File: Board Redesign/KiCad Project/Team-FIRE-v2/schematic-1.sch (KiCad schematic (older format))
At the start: 32 parts, among them J1 SIM_Card, J2 53885-0408, U2 NCN4555MN, U3 CSD18543Q3A

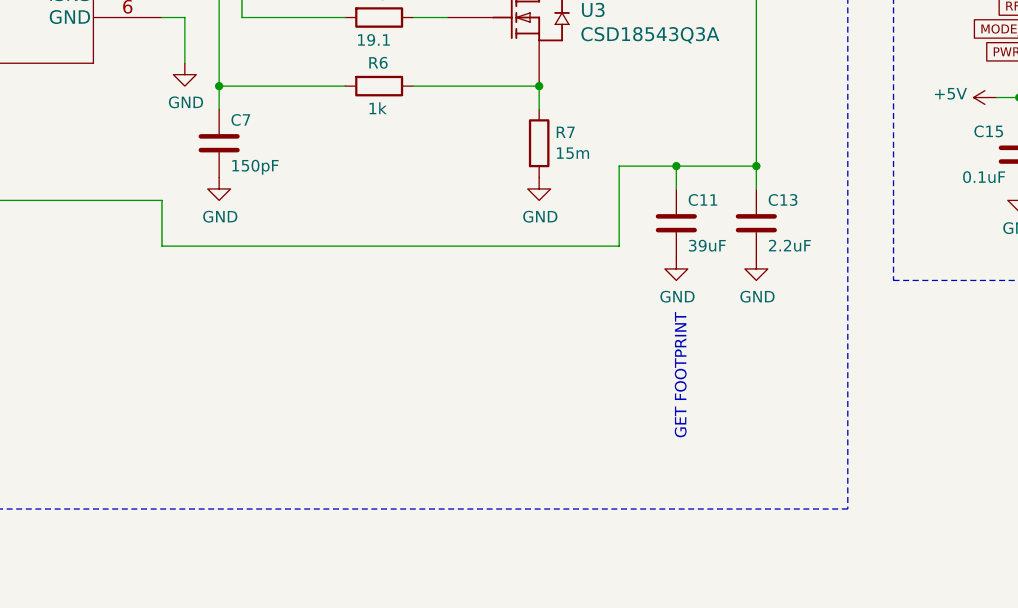
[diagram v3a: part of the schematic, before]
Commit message: Added EEE-FK1H390SV
- Created EEE-FK1H390SV symbol and footprint
- Added EEE-FK1H390SV to Team-FIRE libraries
- Added EEE-FK1H390SV to 8 to 30V boost circuit
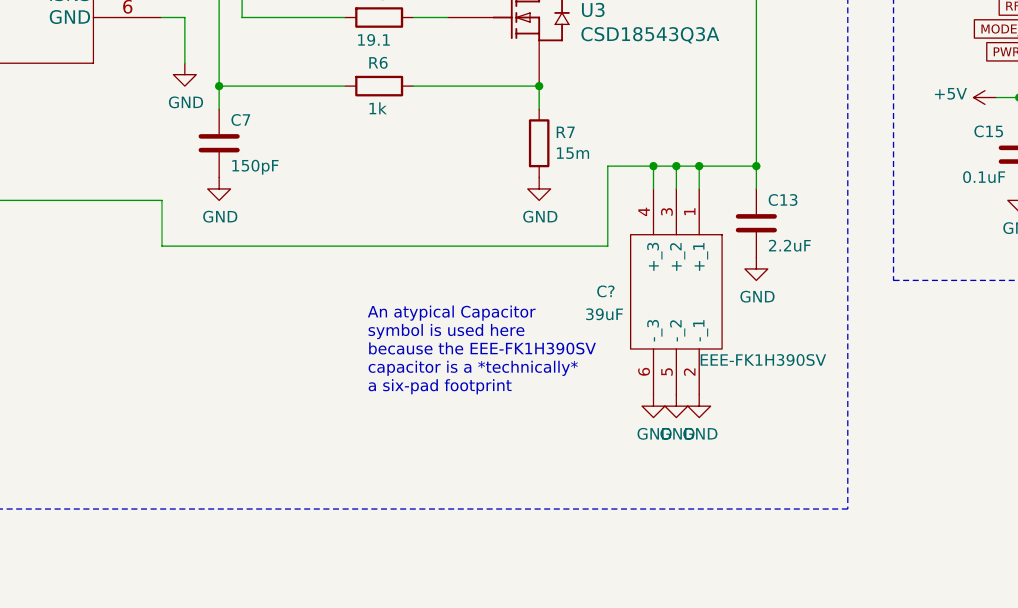
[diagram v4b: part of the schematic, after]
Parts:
- removed C11: 39uF, symbol Device:C
- added C?: 39uF, Team-FIRE:EEEFK1H390SV, symbol Team-FIRE:EEE-FK1H390SV
- C13: Link (none) -> https://www.mouser.com/ProductDetail/Murata-Electronics/GRM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; MPN (none) -> GRM188R61H225KE11D; Manufacturer (none) -> Murata; Supplier (none) -> Mouser; Supplier PN (none) -> 81-GRM188R61H225KE1D; Type (none) -> Ceramic X5R Capacitor; Voltage Rating (none) -> 50 VDC
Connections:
- net GND: now also C?.2 (-_1), C?.5 (-_2), C?.6 (-_3)
- net at C13.1, D1.1 (K), R4.2: now also C?.1 (+_1), C?.3 (+_2), C?.4 (+_3)
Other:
- note added: "An atypical Capacitor\nsymbol is used here\nbecause the EEE-FK1H390SV\ncapacitor is a *technically*\na six-pad footprint"
- note removed: "GET FOOTPRINT"
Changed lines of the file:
@@
-$EndComp
-$Comp
-L Device:C C11
-U 1 1 5ED7F879
-P 6100 3550
-F 0 "C11" H 6150 3650 50  0000 L CNN
-F 1 "39uF" H 6150 3450 50  0000 L CNN
-F 2 "" H 6138 3400 50  0001 C CNN
-F 3 "https://www.mouser.com/datasheet/2/315/ABA0000C1247-1144552.pdf" H 6100 3550 50  0001 C CNN
-F 4 "EEE-FK1H390SV" H 6100 3550 50  0001 C CNN "MPN"
-F 5 "Panasonic" H 6100 3550 50  0001 C CNN "Manufacturer"
-F 6 "Mouser" H 6100 3550 50  0001 C CNN "Supplier"
-F 7 "667-EEE-FK1H390SV" H 6100 3550 50  0001 C CNN "Supplier PN"
-F 8 "https://www.mouser.com/ProductDetail/Panasonic/EEE-FK1H390SV?qs=sGAEpiMZZMsh%252B1woXyUXj34sxNWs20QAUY71LHOgMEw%3D" H 6100 3550 50  0001 C CNN "Link"
-F 9 "Aluminum Electrolytic Capacitors" H 6100 3550 50  0001 C CNN "Type"
-F 10 "20%" H 6100 3550 50  0001 C CNN "Tolerance"
-F 11 "50 VDC" H 6100 3550 50  0001 C CNN "Voltage Rating"
-F 12 "AEC-Q200" H 6100 3550 50  0001 C CNN "Qualification"
-	1    6100 3550
-	1    0    0    -1
 $EndComp
 $Comp
@@
 F 1 "2.2uF" H 6500 3450 50  0000 L CNN
 F 2 "Capacitor_SMD:C_0603_1608Metric" H 6488 3400 50  0001 C CNN
-F 3 "~" H 6450 3550 50  0001 C CNN
+F 3 "https://www.mouser.com/datasheet/2/281/murata_03052018_GRM_Series_1-1310166.pdf" H 6450 3550 50  0001 C CNN
+F 4 "GRM188R61H225KE11D" H 6450 3550 50  0001 C CNN "MPN"
+F 5 "Murata" H 6450 3550 50  0001 C CNN "Manufacturer"
+F 6 "Mouser" H 6450 3550 50  0001 C CNN "Supplier"
+F 7 "81-GRM188R61H225KE1D" H 6450 3550 50  0001 C CNN "Supplier PN"
+F 8 "https://www.mouser.com/ProductDetail/Murata-Electronics/GRM188R61H225KE11D?qs=sGAEpiMZZMs0AnBnWHyRQKFZIQ7b73cd5p1cvIMBXrTOTAbV%2F8mfyA%3D%3D" H 6450 3550 50  0001 C CNN "Link"
+F 9 "Ceramic X5R Capacitor" H 6450 3550 50  0001 C CNN "Type"
+F 10 "50 VDC" H 6450 3550 50  0001 C CNN "Voltage Rating"
 	1    6450 3550
 	1    0    0    -1
@@
 L power:GND #PWR0123
 U 1 1 5ED80FA2
-P 6100 3700
-F 0 "#PWR0123" H 6100 3450 50  0001 C CNN
-F 1 "GND" H 6105 3527 50  0000 C CNN
-F 2 "" H 6100 3700 50  0001 C CNN
-F 3 "" H 6100 3700 50  0001 C CNN
-	1    6100 3700
+P 6100 4300
+F 0 "#PWR0123" H 6100 4050 50  0001 C CNN
+F 1 "GND" H 6105 4127 50  0000 C CNN
+F 2 "" H 6100 4300 50  0001 C CNN
+F 3 "" H 6100 4300 50  0001 C CNN
+	1    6100 4300
 	1    0    0    -1
 $EndComp
@@
 Connection ~ 6100 3300
 Wire Wire Line
-	6100 3300 6450 3300
+	6100 3300 6200 3300
 Wire Wire Line
 	6200 2200 6450 2200
@@
 Wire Wire Line
 	3950 2650 3850 2650
-Text Notes 6150 4500 1    50   ~ 0
-GET FOOTPRINT
 Connection ~ 4100 2950
 Wire Wire Line
@@
 	3850 3450 3850 3650
 Wire Wire Line
-	3850 3650 5850 3650
-Wire Wire Line
-	5850 3650 5850 3300
-Wire Wire Line
-	5850 3300 6100 3300
+	3850 3650 5800 3650
+Wire Wire Line
+	5800 3650 5800 3300
 Wire Wire Line
 	2650 3450 3850 3450
@@
 Text Notes 5450 6100 2    50   ~ 0
 FIND COMPONENT
+$Comp
+L Team-FIRE:EEE-FK1H390SV C?
+U 1 1 5EAA6D91
+P 6500 3400
+F 0 "C?" V 6950 2650 50  0000 L CNN
+F 1 "39uF" V 7050 2600 50  0000 L CNN
+F 2 "Team-FIRE:EEEFK1H390SV" H 7250 3500 50  0001 L CNN
+F 3 "https://b2b-api.panasonic.eu/file_stream/pids/fileversion/3102" H 7250 3400 50  0001 L CNN
+F 4 "667-EEE-FK1H390SV" H 7250 3100 50  0001 L CNN "Supplier PN"
+F 5 "Panasonic" H 7250 2900 50  0001 L CNN "Manufacturer"
+F 6 "EEE-FK1H390SV" V 7250 3100 50  0000 L CNN "MPN"
+F 7 "Digikey" H 6500 3400 50  0001 C CNN "Supplier"
+F 8 "https://www.digikey.com/product-detail/en/panasonic-electronic-components/EEE-FK1H390SV/P124697CT-ND/10290639" H 6500 3400 50  0001 C CNN "Link"
+F 9 "Aluminum Electrolytic Capacitor" H 6500 3400 50  0001 C CNN "Type"
+F 10 "20%" H 6500 3400 50  0001 C CNN "Tolerance"
+F 11 "50 VDC" H 6500 3400 50  0001 C CNN "Voltage Rating"
+	1    6500 3400
+	0    1    1    0
+$EndComp
+Wire Wire Line
+	6000 3400 6000 3300
+Connection ~ 6000 3300
+Wire Wire Line
+	6000 3300 6100 3300
+Wire Wire Line
+	6200 3400 6200 3300
+Connection ~ 6200 3300
+Wire Wire Line
+	6200 3300 6450 3300
+$Comp
+L power:GND #PWR?
+U 1 1 5EAC5511
+P 6000 4300
+F 0 "#PWR?" H 6000 4050 50  0001 C CNN
+F 1 "GND" H 6005 4127 50  0000 C CNN
+F 2 "" H 6000 4300 50  0001 C CNN
+F 3 "" H 6000 4300 50  0001 C CNN
+	1    6000 4300
+	1    0    0    -1
+$EndComp
+$Comp
+L power:GND #PWR?
+U 1 1 5EAC5A93
+P 6200 4300
+F 0 "#PWR?" H 6200 4050 50  0001 C CNN
+F 1 "GND" H 6205 4127 50  0000 C CNN
+F 2 "" H 6200 4300 50  0001 C CNN
+F 3 "" H 6200 4300 50  0001 C CNN
+	1    6200 4300
+	1    0    0    -1
+$EndComp
+Text Notes 4750 4300 0    50   ~ 0
+An atypical Capacitor\nsymbol is used here\nbecause the EEE-FK1H390SV\ncapacitor is a *technically*\na six-pad footprint
+Wire Wire Line
+	5800 3300 6000 3300
 $EndSCHEMATC

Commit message: Made a lot of changes...
- Added symbol, footprint for Micro USB B connector
- Fixed Flash Memory schematic
- Added details for many components
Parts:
- gave numbers to parts that had none: 4
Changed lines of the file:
@@
 	10550 1200 10650 1200
 $Comp
-L Team-FIRE:TPS40210DGQR U?
+L Team-FIRE:TPS40210DGQR U1
 U 1 1 5EAFAF05
 P 1850 2250
-F 0 "U?" H 2850 2637 60  0000 C CNN
+F 0 "U1" H 2850 2637 60  0000 C CNN
 F 1 "TPS40210DGQR" H 2850 2531 60  0000 C CNN
 F 2 "Team-FIRE:TPS40210DGQR" H 2950 2450 60  0001 C CNN
@@
 P 8900 5200
 AR Path="/5F173878" Ref="C?"  Part="1"
-AR Path="/5E4D0D8F/5F173878" Ref="C?"  Part="1"
+AR Path="/5E4D0D8F/5F173878" Ref="C12"  Part="1"
 AR Path="/5E759307/5F173878" Ref="C?"  Part="1"
-F 0 "C?" H 8750 5300 50  0000 L CNN
+F 0 "C12" H 8750 5300 50  0000 L CNN
 F 1 "1uF" H 8750 5100 50  0000 L CNN
 F 2 "Capacitor_SMD:C_0603_1608Metric" H 8938 5050 50  0001 C CNN
@@
 $EndComp
 $Comp
-L Device:C C?
+L Device:C C14
 U 1 1 5F174FB5
 P 9200 5200
-F 0 "C?" H 9250 5300 50  0000 L CNN
+F 0 "C14" H 9250 5300 50  0000 L CNN
 F 1 "10uF" H 9250 5100 50  0000 L CNN
 F 2 "Capacitor_SMD:C_0603_1608Metric" H 9238 5050 50  0001 C CNN
@@
 FIND COMPONENT
 $Comp
-L Team-FIRE:EEE-FK1H390SV C?
+L Team-FIRE:EEE-FK1H390SV C11
 U 1 1 5EAA6D91
 P 6500 3400
-F 0 "C?" V 6950 2650 50  0000 L CNN
+F 0 "C11" V 6950 2650 50  0000 L CNN
 F 1 "39uF" V 7050 2600 50  0000 L CNN
 F 2 "Team-FIRE:EEEFK1H390SV" H 7250 3500 50  0001 L CNN
@@
 	6200 3300 6450 3300
 $Comp
-L power:GND #PWR?
+L power:GND #PWR01
 U 1 1 5EAC5511
 P 6000 4300
-F 0 "#PWR?" H 6000 4050 50  0001 C CNN
+F 0 "#PWR01" H 6000 4050 50  0001 C CNN
 F 1 "GND" H 6005 4127 50  0000 C CNN
 F 2 "" H 6000 4300 50  0001 C CNN
@@
 $EndComp
 $Comp
-L power:GND #PWR?
+L power:GND #PWR02
 U 1 1 5EAC5A93
 P 6200 4300
-F 0 "#PWR?" H 6200 4050 50  0001 C CNN
+F 0 "#PWR02" H 6200 4050 50  0001 C CNN
 F 1 "GND" H 6205 4127 50  0000 C CNN
 F 2 "" H 6200 4300 50  0001 C CNN

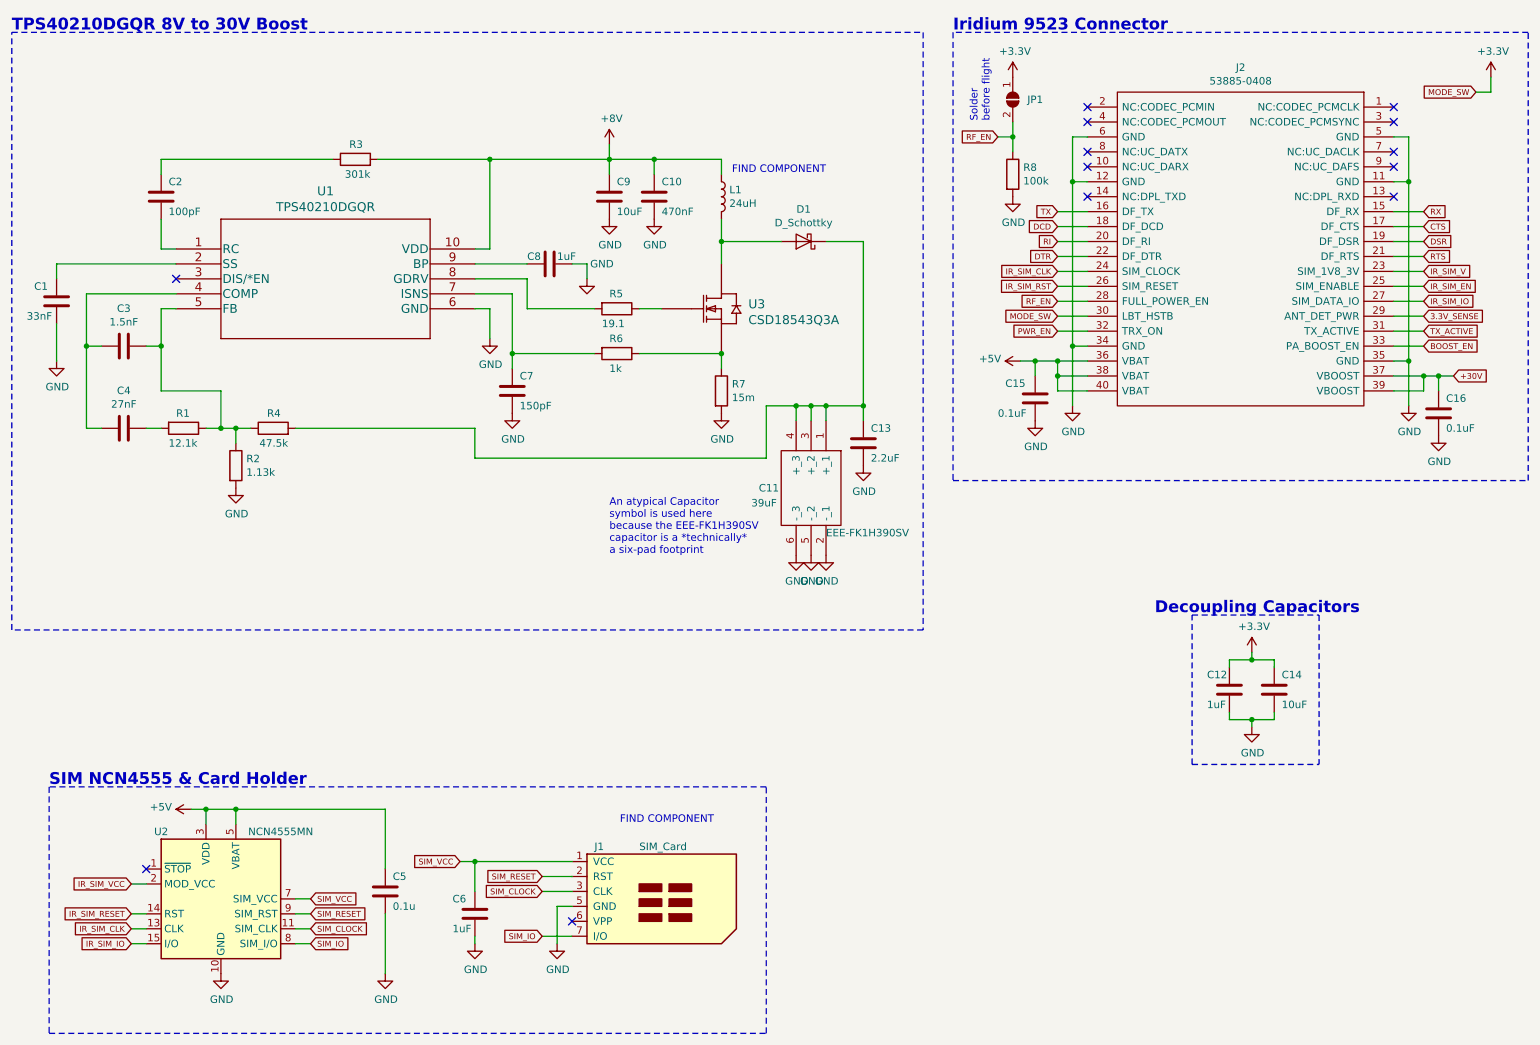
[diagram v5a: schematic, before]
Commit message: Labelled finished sections on schematic, picked LEDs
- Labelled all finished schematic sections if they've been part-selected / verified (and by whom)
- Selected the four debug LEDs and filled out BOM info
- Filled out info for Power/TES connectors
- Filled out info for RF connector
- Filled out info for 5 to 3.3V regulator
- Filled out info for 8 to 5V switching regulator
- Assigned footprints to test points
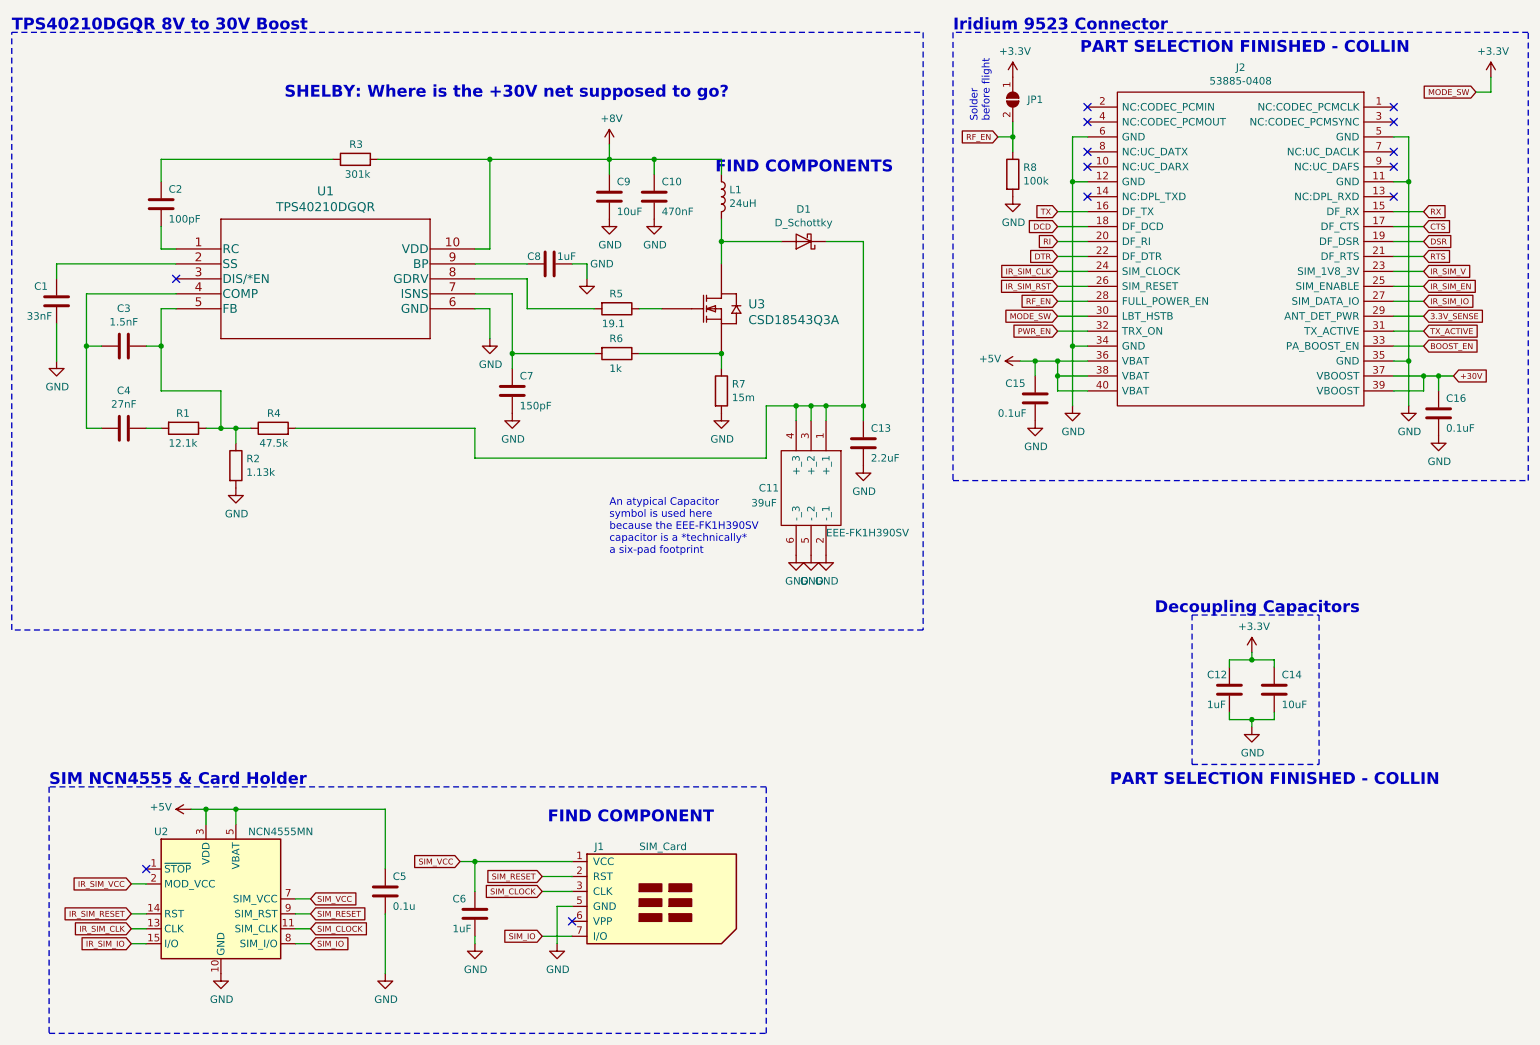
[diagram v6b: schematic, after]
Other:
- note added: "FIND COMPONENTS"
- note added: "PART SELECTION FINISHED - COLLIN"
- note added: "SHELBY: Where is the +30V net supposed to go?"
- moved on the sheet: C2
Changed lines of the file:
@@
 L Device:C C2
 U 1 1 5EA803DA
-P 1750 1900
-F 0 "C2" H 1800 2000 50  0000 L CNN
-F 1 "100pF" H 1800 1800 50  0000 L CNN
-F 2 "Capacitor_SMD:C_0603_1608Metric" H 1788 1750 50  0001 C CNN
-F 3 "~" H 1750 1900 50  0001 C CNN
-F 4 "CBR06C101F5GAC" H 1750 1900 50  0001 C CNN "MPN"
-F 5 "KEMET" H 1750 1900 50  0001 C CNN "Manufacturer"
-F 6 "https://www.mouser.com/ProductDetail/KEMET/CBR06C101F5GAC?qs=sGAEpiMZZMs0AnBnWHyRQN7%2FAA2D2lPPUdZo0nHgvrj7UthX3WhjQw%3D%3D" H 1750 1900 50  0001 C CNN "Link"
-F 7 "80-CBR06C101F5GAC" H 1750 1900 50  0001 C CNN "Supplier PN"
-F 8 "Ceramic C0G Capacitor" H 1750 1900 50  0001 C CNN "Type"
-F 9 "1%" H 1750 1900 50  0001 C CNN "Tolerance"
-F 10 "50 VDC" H 1750 1900 50  0001 C CNN "Voltage Rating"
-	1    1750 1900
+P 1750 1950
+F 0 "C2" H 1800 2050 50  0000 L CNN
+F 1 "100pF" H 1800 1850 50  0000 L CNN
+F 2 "Capacitor_SMD:C_0603_1608Metric" H 1788 1800 50  0001 C CNN
+F 3 "~" H 1750 1950 50  0001 C CNN
+F 4 "CBR06C101F5GAC" H 1750 1950 50  0001 C CNN "MPN"
+F 5 "KEMET" H 1750 1950 50  0001 C CNN "Manufacturer"
+F 6 "https://www.mouser.com/ProductDetail/KEMET/CBR06C101F5GAC?qs=sGAEpiMZZMs0AnBnWHyRQN7%2FAA2D2lPPUdZo0nHgvrj7UthX3WhjQw%3D%3D" H 1750 1950 50  0001 C CNN "Link"
+F 7 "80-CBR06C101F5GAC" H 1750 1950 50  0001 C CNN "Supplier PN"
+F 8 "Ceramic C0G Capacitor" H 1750 1950 50  0001 C CNN "Type"
+F 9 "1%" H 1750 1950 50  0001 C CNN "Tolerance"
+F 10 "50 VDC" H 1750 1950 50  0001 C CNN "Voltage Rating"
+	1    1750 1950
 	1    0    0    -1
 $EndComp
@@
 	1850 2250 1750 2250
 Wire Wire Line
-	1750 2250 1750 2050
-Wire Wire Line
-	1750 1750 1750 1650
-Wire Wire Line
 	1750 1650 2900 1650
 Wire Wire Line
@@
 	1    0    0    -1
 $EndComp
-Text Notes 6200 1750 2    50   ~ 0
-FIND COMPONENT
-Text Notes 5450 6100 2    50   ~ 0
+Text Notes 6650 1750 2    79   ~ 16
+FIND COMPONENTS
+Text Notes 5450 6100 2    79   ~ 16
 FIND COMPONENT
 $Comp
@@
 Wire Wire Line
 	5800 3300 6000 3300
+Wire Wire Line
+	1750 1650 1750 1800
+Wire Wire Line
+	1750 2100 1750 2250
+Text Notes 5550 1250 2    79   ~ 16
+SHELBY: Where is the +30V net supposed to go?
+Text Notes 8100 5850 0    79   ~ 16
+PART SELECTION FINISHED - COLLIN
+Text Notes 7900 950  0    79   ~ 16
+PART SELECTION FINISHED - COLLIN
 $EndSCHEMATC
